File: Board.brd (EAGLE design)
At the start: 100 x 100 mm, 148 parts, among them U2 MAX7219CWG, U3 MAX7219CWG

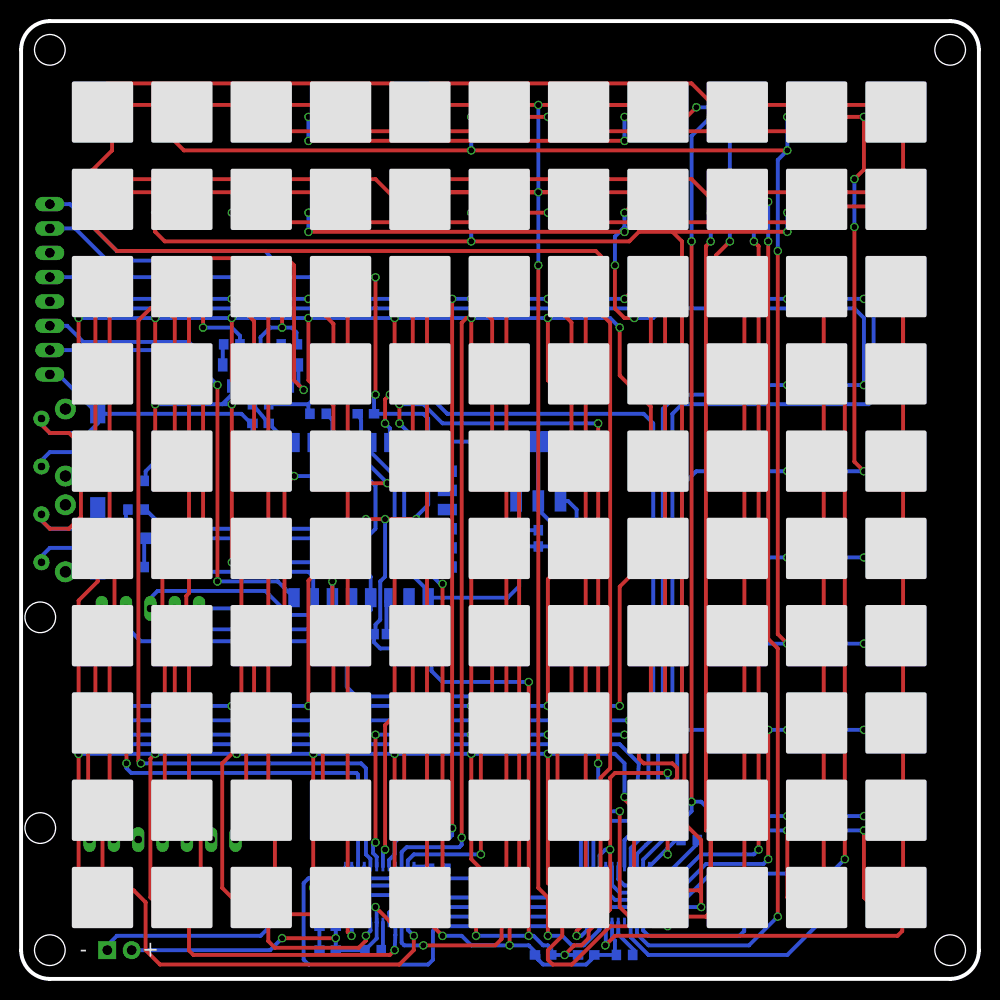
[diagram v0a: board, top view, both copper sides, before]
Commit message: fixed wrong footprint for MAX7219
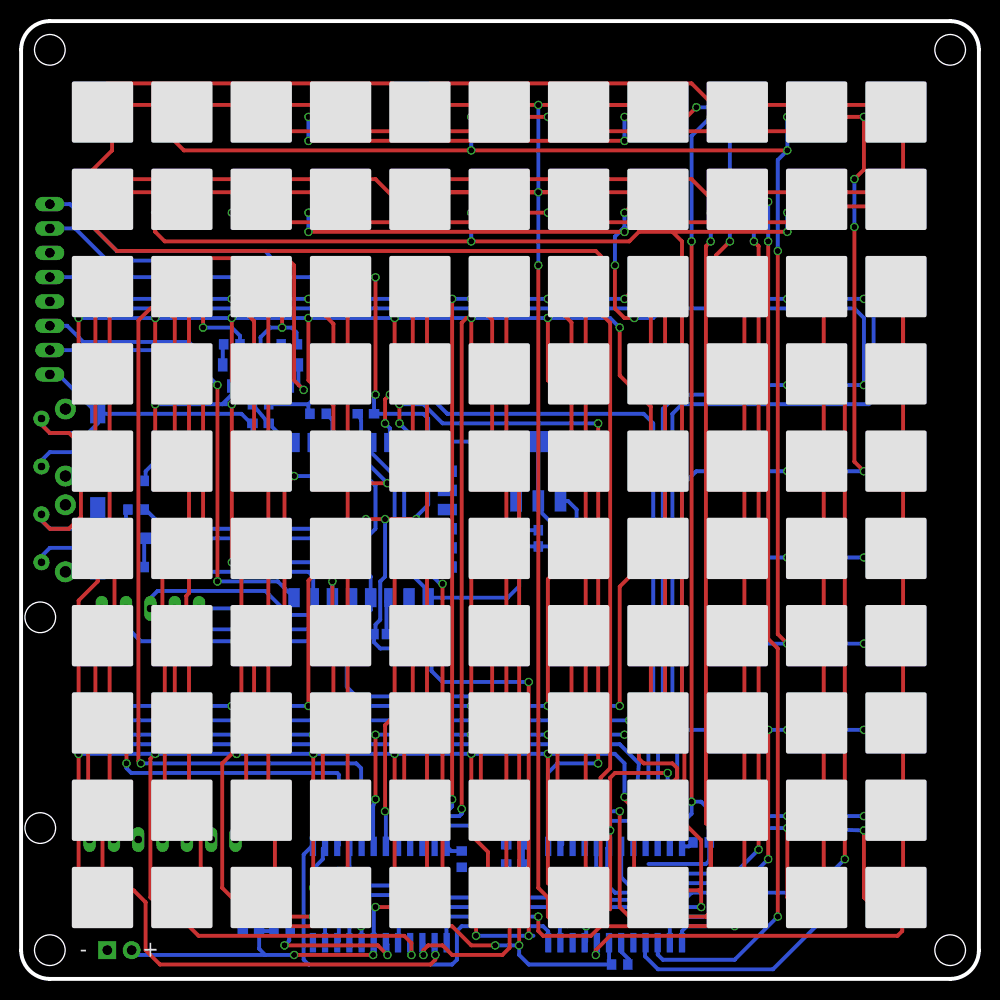
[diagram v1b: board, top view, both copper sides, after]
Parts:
- U2, U3: device maxim:TSSOP24 -> max7219:SO24L
- moved C2 12.1 mm to (51.5, 12.0)
- moved C1 11.9 mm to (51.5, 14.0), turned to 0 degrees
- moved R1 9.71 mm to (27.2, 5.00)
- moved C4 8.25 mm to (24.0, 5.00)
- moved C3 8.14 mm to (24.0, 7.00)
- moved R2 2.69 mm to (46.0, 12.5), turned to 90 degrees
- moved R4 1.27 mm to (71.0, 14.2)
- moved R3 1.12 mm to (62.5, 1.50)
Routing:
- net GND: track 311.7 -> 259.9 mm, vias 13 -> 12
- net N$43: track 3.01 -> 14.2 mm, vias 0 -> 2
- net +5V: track 165.9 -> 173.3 mm, vias 7 -> 8
- net CLK: track 90.4 -> 95.5 mm
- net N$8: track 252.9 -> 248.5 mm
- net N$2: track 136.1 -> 131.8 mm
- net N$16: track 114.1 -> 118.3 mm
- net N$7: track 232.0 -> 227.9 mm
- net LOAD: track 91.2 -> 87.2 mm
- net N$13: track 73.0 -> 76.6 mm
- net N$35: track 46.4 -> 42.9 mm
- net N$4: track 82.5 -> 79.1 mm
- net N$25: track 79.9 -> 76.6 mm
- net N$17: track 183.5 -> 180.2 mm
- net N$23: track 188.2 -> 191.3 mm
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
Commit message: increased font size for silk screen
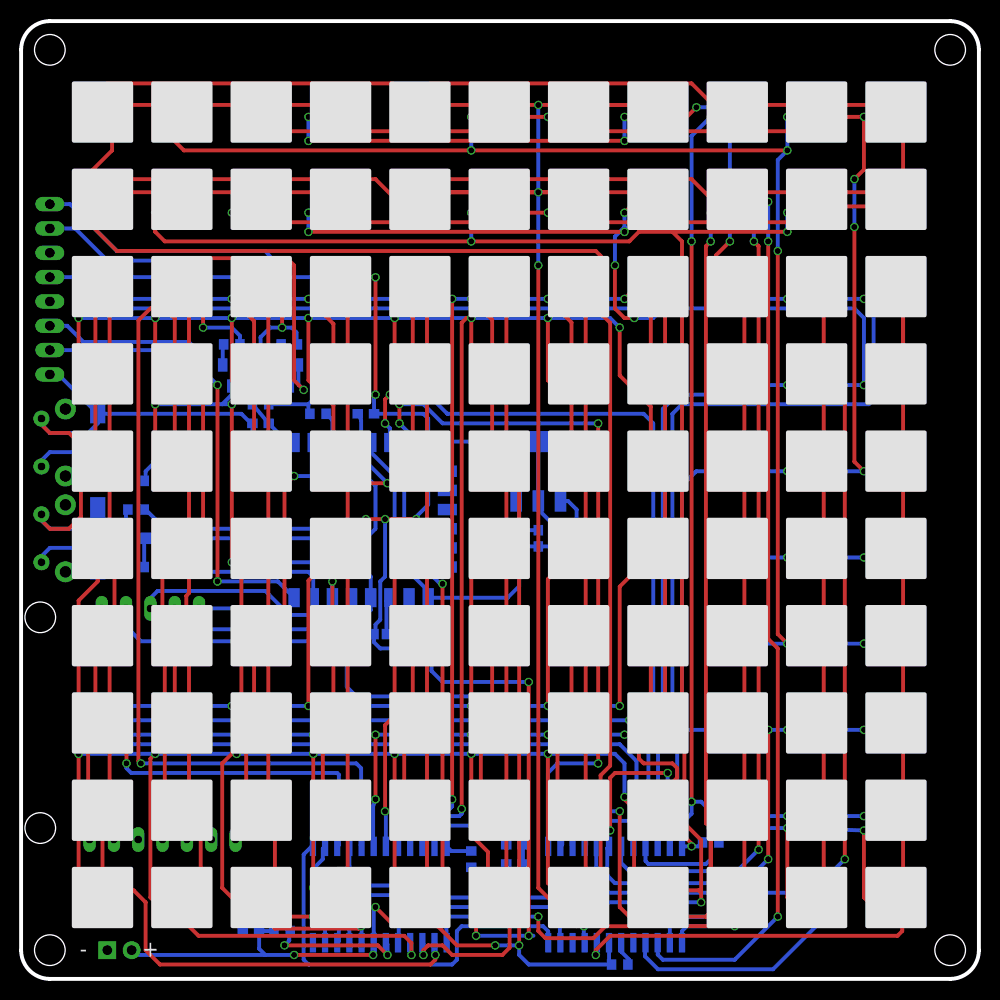
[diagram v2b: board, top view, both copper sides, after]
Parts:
- moved R2 1.00 mm to (47.0, 12.5)
- moved R4 1.00 mm to (72.0, 14.2)
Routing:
- net GND: track 259.9 -> 251.7 mm
- net N$20: track 193.8 -> 191.6 mm
- net N$29: track 169.2 -> 167.7 mm
- net N$19: track 195.3 -> 193.8 mm
- net LOAD: track 87.2 -> 88.6 mm
- net N$23: track 191.3 -> 190.3 mm
- net N$33: track 1.77 -> 2.77 mm
- net N$16: track 118.3 -> 117.5 mm
- net N$28: track 199.3 -> 199.8 mm
